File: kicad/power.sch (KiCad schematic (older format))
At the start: 65 parts, among them U701 TPS62420DRCR

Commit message: cleaning power, added ac/dc to 15v
I've added the ac/dc power supply based on encapsulated off load power
supply and chainde linear regulator for 5, 3v3 and 1v2 for cold gnd and
5v and 3v3 for hot gnd.
I'll next join some sheet 'cose some of those are almost empty
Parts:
- removed C705, C713, C717: 0.1uF, symbol servo:Capacitor
- removed C709, C731, C735: 22uF, symbol servo:Capacitor
- removed C730: 33pF, symbol servo:Capacitor
- removed D701: MBRM110ET1G, symbol servo:DIODE_SCHOTTKY
- removed D702: CFSH05-20L TR, symbol servo:DIODE_SCHOTTKY
- removed D703: red, symbol servo:LED_A2_K1
- removed L701: 2.2uH, symbol servo:Inductor_Iron
- removed L702: 3.3uH, symbol servo:Inductor_Iron
- removed R701, R703, R706: 0e, symbol servo:Resistor
- removed R702: 22k, symbol servo:Resistor
- removed R704: 10k, symbol servo:Resistor
- removed R705: 100k, symbol servo:Resistor
- removed R707: 205k, symbol servo:Resistor
- removed R708: 200k, symbol servo:Resistor
- removed R709: 340k, symbol servo:Resistor
- removed R710: 2.00k, symbol servo:Resistor
- removed R711: 75.0k, symbol servo:Resistor
- removed R712: 680, symbol servo:Resistor
- removed TP701, TP702, TP703, TP704: ~, symbol servo:CMP-0078143-2
- removed U701: TPS62420DRCR, symbol servo:TPS6240x
- U1_701: symbol servo:TMS320F28388_5 -> servo:TMS320F28388
- U1_702: symbol servo:TMS320F28388_4 -> servo:TMS320F28388
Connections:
- net labels added: 1V2C, 3V3C
- net labels removed: 1V2, 3V3, HSEC_5V0, IN_5V0, USB_5V0
- wire segments 340 -> 263
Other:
- note removed: "1.2V and 3.3V Supplies"

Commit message: ok, it's enough cleaned to mix with power interface
I think it's time to mix with power interfaces.. It's enough cleaned
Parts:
- removed C732, C733, C736, C737: 2.2uF, symbol servo:Capacitor
- removed C734, C738: 10uF, symbol servo:Capacitor
- removed L703, L704: 60 ohm, symbol servo:Ferrite_Bead
- removed L705: 220 ohm, symbol servo:Ferrite_Bead
- added C? (x2): 10uF, symbol servo:Capacitor
- added C? (x4): 2.2uF, symbol servo:Capacitor
- added L? (x2): 60 ohm, symbol servo:Ferrite_Bead
- added L?: 220 ohm, symbol servo:Ferrite_Bead
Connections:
- net labels added: 1V2, 3V3, 3V3A, GNDA, IN_1V2C, IN_3V3C
- net labels removed: 1V2C, 3V3C, VDDA_3V3, VDD_1V2, VDD_3V3
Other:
- moved on the sheet: C701, C702, C703, C704, C706, C707, C708, C710, C711, C712, C714, C715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

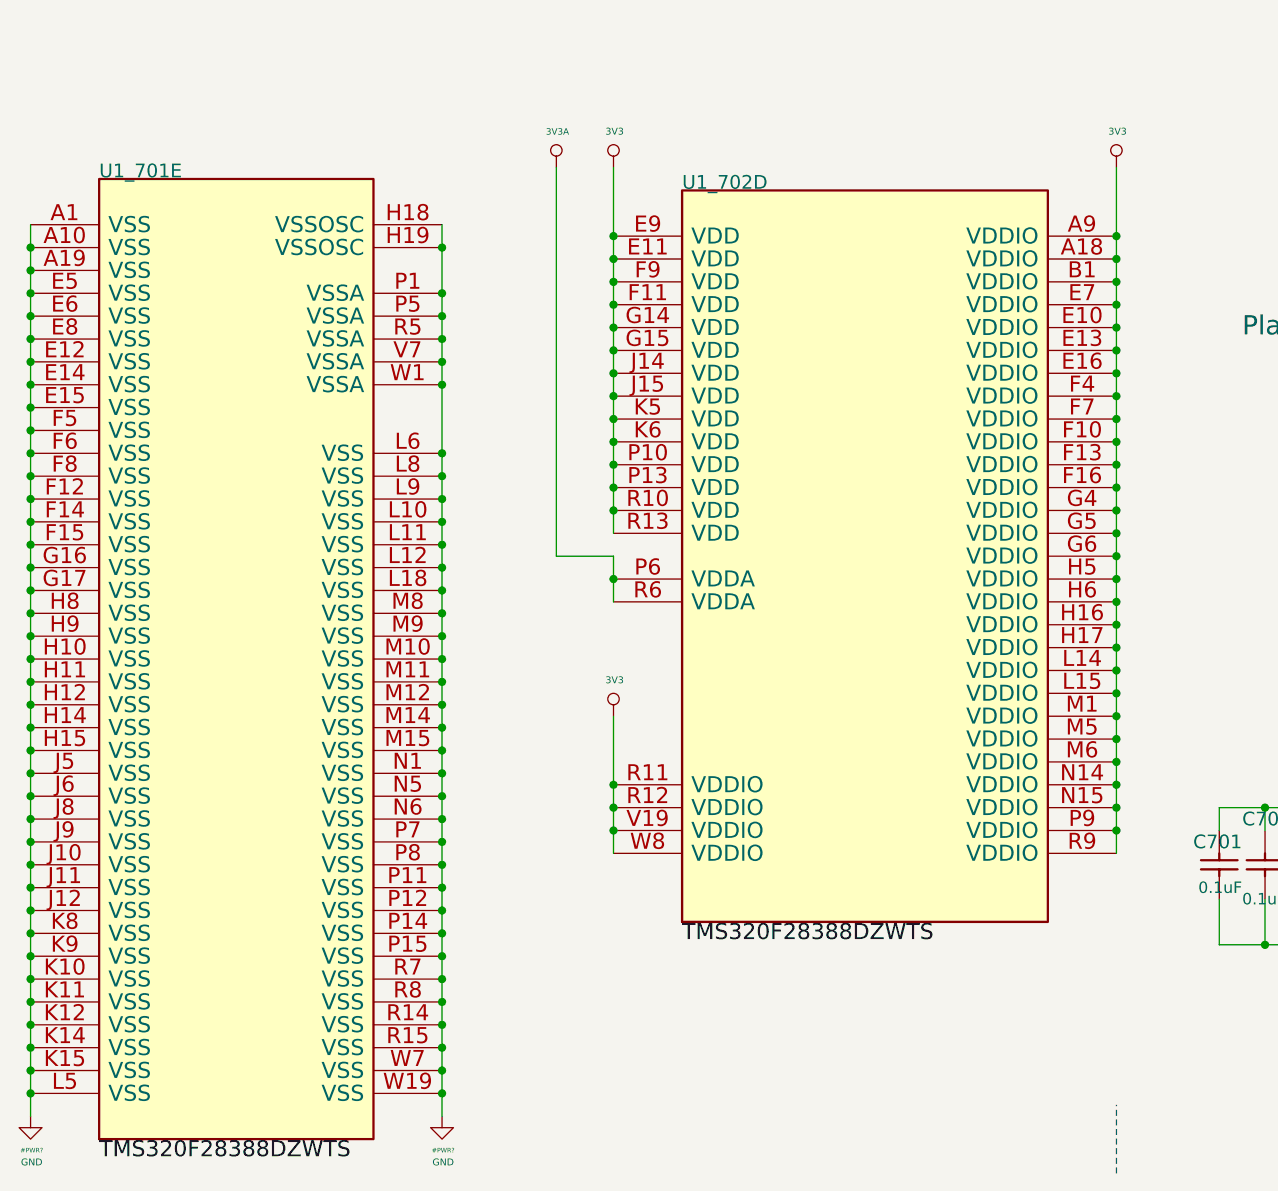
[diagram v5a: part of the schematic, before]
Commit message: added igbt interface, lem, and impprove root page
improved root page, added lem using hall sensor instead shunt, add
somthing on adc page, and ac input.. keep working
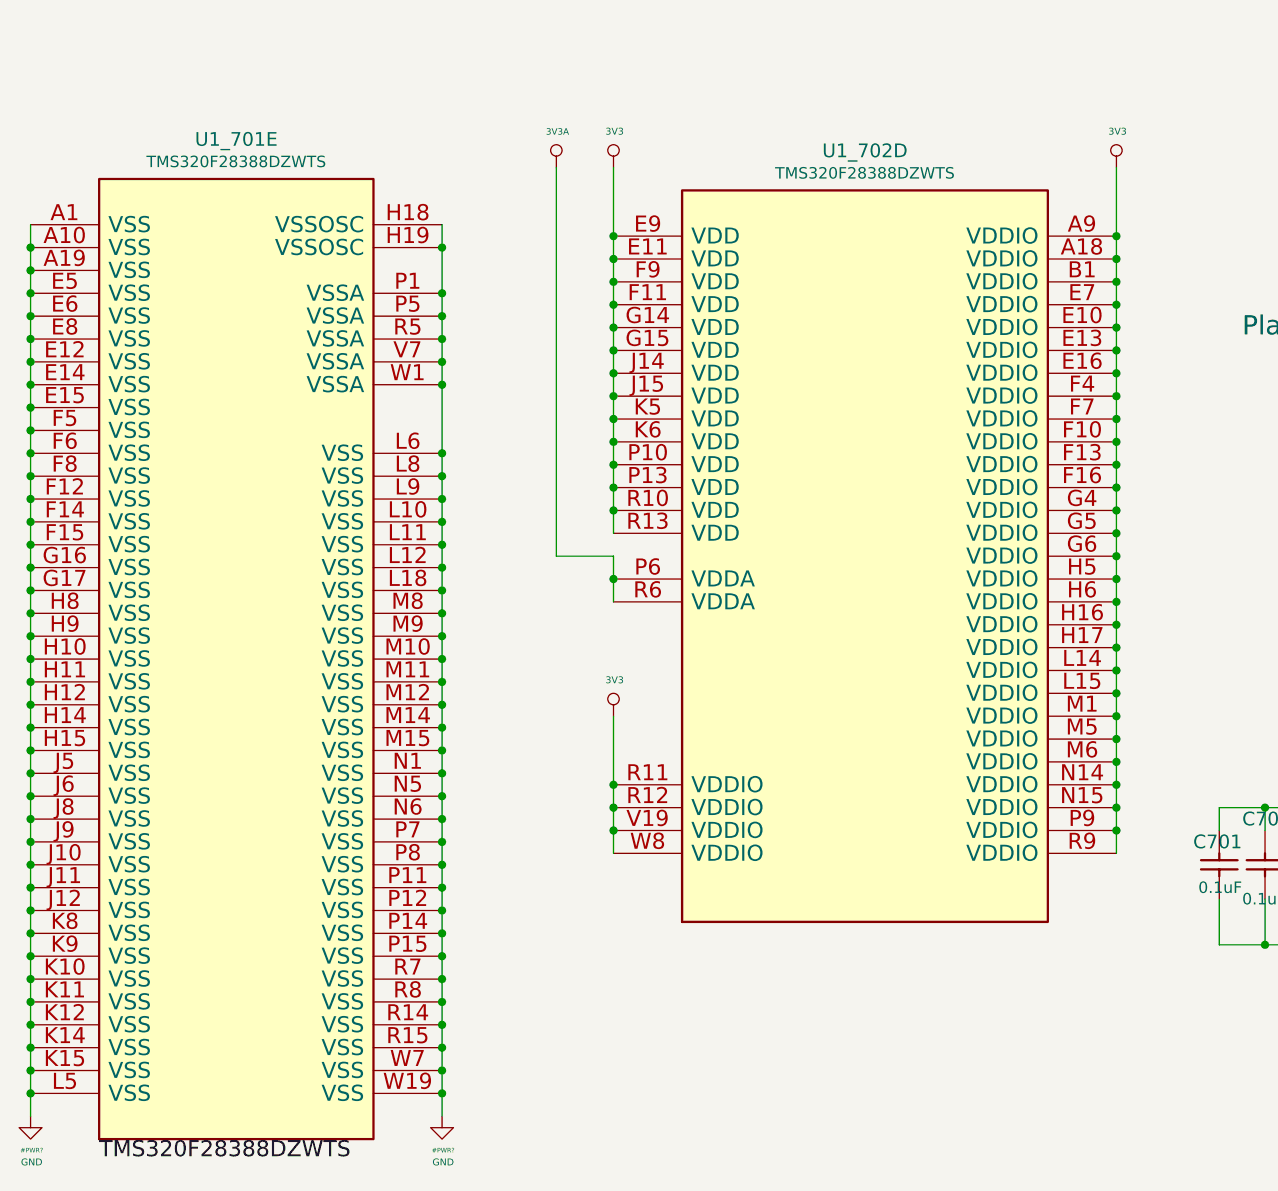
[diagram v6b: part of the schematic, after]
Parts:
- U1_701, U1_702: value ~ -> TMS320F28388DZWTS

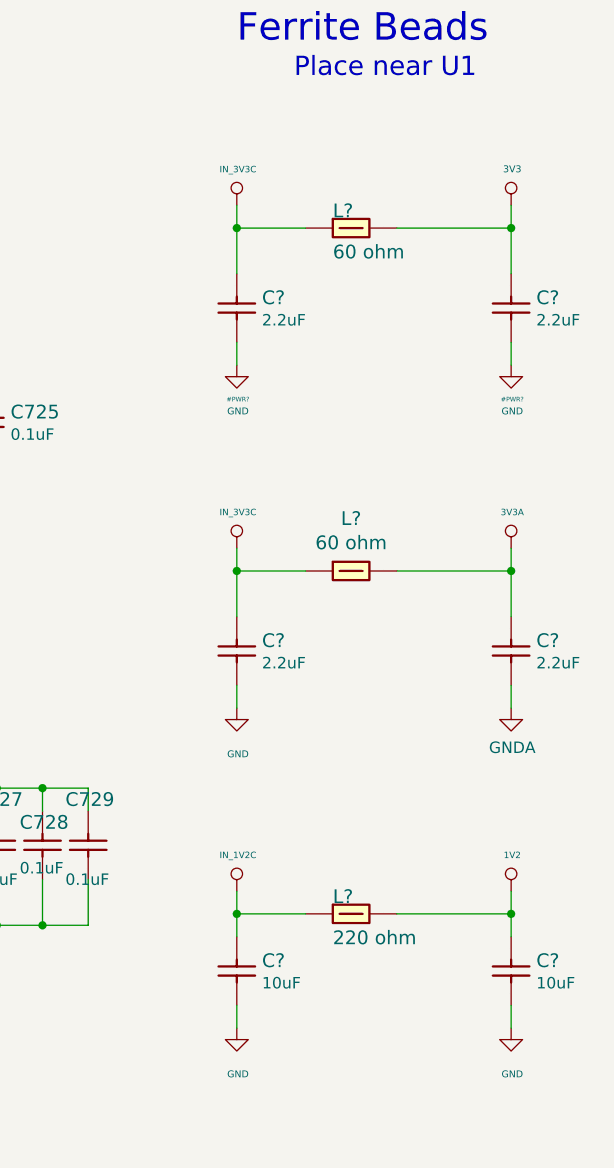
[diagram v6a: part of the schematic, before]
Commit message: I've connected interfaces to gpio and change some muxes
I've changed some muxes reading the datasheet to group same kind of
signals, now it's time to add encoders input
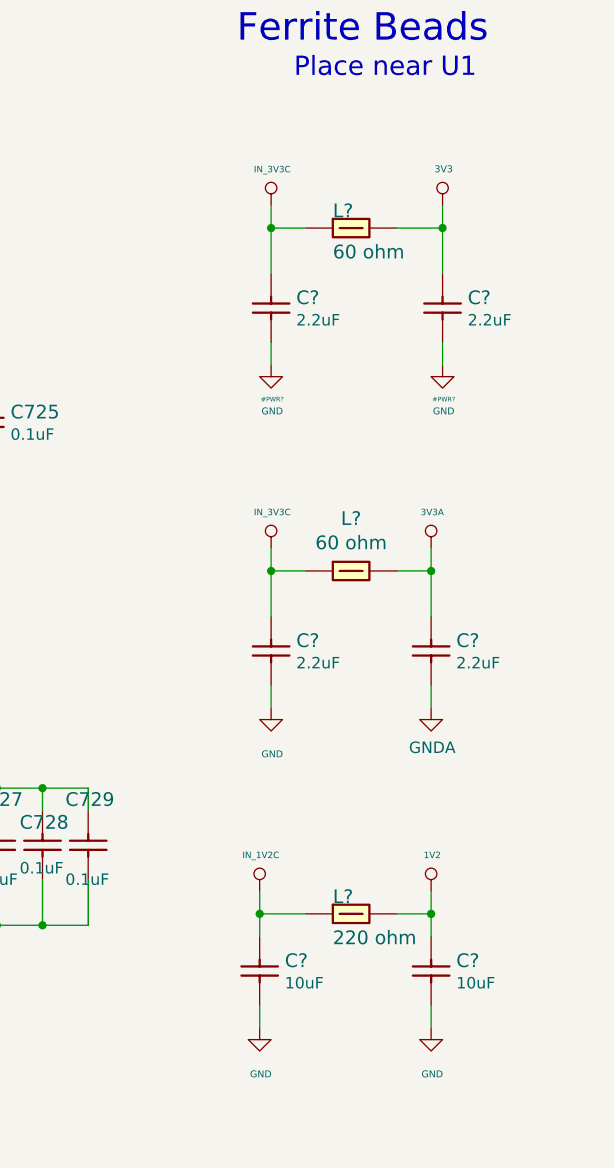
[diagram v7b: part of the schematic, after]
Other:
- moved on the sheet: C?
